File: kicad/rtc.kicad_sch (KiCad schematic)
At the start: 6 parts, among them U1007 AM1805, Y1004 Crystal

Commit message: unify module and board
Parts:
- renumbered C1040 to C37, C1041 to C38, C1042 to C39, C1043 to C40, U1007 to U12, Y1004 to Y2
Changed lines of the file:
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@@
 		(dnp no)
 		(fields_autoplaced yes)
-		(property "Reference" "C1041"
+		(property "Reference" "C38"
 			(at 117.221 57.5853 0)
 			(effects
@@
 			(project "riotee-module"
 				(path "/e235c9a3-080d-42b7-93df-883e69095a9f/1e27cf53-0710-4019-b3d0-1fa374a39b5a/71a24394-376e-48cc-9057-ddfdf0a39757/0e9955bb-beb0-499a-aac5-d497982d12cc"
-					(reference "C1041")
+					(reference "C38")
 					(unit 1)
 				)
@@
 		(on_board yes)
 		(dnp no)
-		(property "Reference" "C1042"
+		(property "Reference" "C39"
 			(at 107.95 96.52 0)
 			(effects
@@
 			(project "riotee-module"
 				(path "/e235c9a3-080d-42b7-93df-883e69095a9f/1e27cf53-0710-4019-b3d0-1fa374a39b5a/71a24394-376e-48cc-9057-ddfdf0a39757/0e9955bb-beb0-499a-aac5-d497982d12cc"
-					(reference "C1042")
+					(reference "C39")
 					(unit 1)
 				)
@@
 		(dnp no)
 		(fields_autoplaced yes)
-		(property "Reference" "C1043"
+		(property "Reference" "C40"
 			(at 180.721 57.5853 0)
 			(effects
@@
 			(project "riotee-module"
 				(path "/e235c9a3-080d-42b7-93df-883e69095a9f/1e27cf53-0710-4019-b3d0-1fa374a39b5a/71a24394-376e-48cc-9057-ddfdf0a39757/0e9955bb-beb0-499a-aac5-d497982d12cc"
-					(reference "C1043")
+					(reference "C40")
 					(unit 1)
 				)
@@
 		(dnp no)
 		(fields_autoplaced yes)
-		(property "Reference" "C1040"
+		(property "Reference" "C37"
 			(at 105.791 57.5853 0)
 			(effects
@@
 			(project "riotee-module"
 				(path "/e235c9a3-080d-42b7-93df-883e69095a9f/1e27cf53-0710-4019-b3d0-1fa374a39b5a/71a24394-376e-48cc-9057-ddfdf0a39757/0e9955bb-beb0-499a-aac5-d497982d12cc"
-					(reference "C1040")
+					(reference "C37")
 					(unit 1)
 				)
@@
 		(dnp no)
 		(fields_autoplaced yes)
-		(property "Reference" "#PWR01048"
+		(property "Reference" "#PWR078"
 			(at 170.18 120.65 0)
 			(effects
@@
 			(project "riotee-module"
 				(path "/e235c9a3-080d-42b7-93df-883e69095a9f/1e27cf53-0710-4019-b3d0-1fa374a39b5a/71a24394-376e-48cc-9057-ddfdf0a39757/0e9955bb-beb0-499a-aac5-d497982d12cc"
-					(reference "#PWR01048")
+					(reference "#PWR078")
 					(unit 1)
 				)
@@
 		(dnp no)
 		(fields_autoplaced yes)
-		(property "Reference" "U1007"
+		(property "Reference" "U12"
 			(at 147.32 54.8472 0)
 			(effects
@@
 			(project "riotee-module"
 				(path "/e235c9a3-080d-42b7-93df-883e69095a9f/1e27cf53-0710-4019-b3d0-1fa374a39b5a/71a24394-376e-48cc-9057-ddfdf0a39757/0e9955bb-beb0-499a-aac5-d497982d12cc"
-					(reference "U1007")
+					(reference "U12")
 					(unit 1)
 				)
@@
 		(on_board yes)
 		(dnp no)
-		(property "Reference" "Y1004"
+		(property "Reference" "Y2"
 			(at 110.9726 82.4484 90)
 			(effects
@@
 			(project "riotee-module"
 				(path "/e235c9a3-080d-42b7-93df-883e69095a9f/1e27cf53-0710-4019-b3d0-1fa374a39b5a/71a24394-376e-48cc-9057-ddfdf0a39757/0e9955bb-beb0-499a-aac5-d497982d12cc"
-					(reference "Y1004")
+					(reference "Y2")
 					(unit 1)
 				)
@@
 		(dnp no)
 		(fields_autoplaced yes)
-		(property "Reference" "#PWR01049"
+		(property "Reference" "#PWR079"
 			(at 177.8 71.12 0)
 			(effects
@@
 			(project "riotee-module"
 				(path "/e235c9a3-080d-42b7-93df-883e69095a9f/1e27cf53-0710-4019-b3d0-1fa374a39b5a/71a24394-376e-48cc-9057-ddfdf0a39757/0e9955bb-beb0-499a-aac5-d497982d12cc"
-					(reference "#PWR01049")
+					(reference "#PWR079")
 					(unit 1)
 				)
@@
 		(dnp no)
 		(fields_autoplaced yes)
-		(property "Reference" "#PWR01045"
+		(property "Reference" "#PWR075"
 			(at 114.3 73.66 0)
 			(effects
@@
 			(project "riotee-module"
 				(path "/e235c9a3-080d-42b7-93df-883e69095a9f/1e27cf53-0710-4019-b3d0-1fa374a39b5a/71a24394-376e-48cc-9057-ddfdf0a39757/0e9955bb-beb0-499a-aac5-d497982d12cc"
-					(reference "#PWR01045")
+					(reference "#PWR075")
 					(unit 1)
 				)
@@
 		(dnp no)
 		(fields_autoplaced yes)
-		(property "Reference" "#PWR01047"
+		(property "Reference" "#PWR077"
 			(at 124.46 120.65 0)
 			(effects
@@
 			(project "riotee-module"
 				(path "/e235c9a3-080d-42b7-93df-883e69095a9f/1e27cf53-0710-4019-b3d0-1fa374a39b5a/71a24394-376e-48cc-9057-ddfdf0a39757/0e9955bb-beb0-499a-aac5-d497982d12cc"
-					(reference "#PWR01047")
+					(reference "#PWR077")
 					(unit 1)
 				)
@@
 		(dnp no)
 		(fields_autoplaced yes)
-		(property "Reference" "#PWR01046"
+		(property "Reference" "#PWR076"
 			(at 114.3 120.65 0)
 			(effects
@@
 			(project "riotee-module"
 				(path "/e235c9a3-080d-42b7-93df-883e69095a9f/1e27cf53-0710-4019-b3d0-1fa374a39b5a/71a24394-376e-48cc-9057-ddfdf0a39757/0e9955bb-beb0-499a-aac5-d497982d12cc"
-					(reference "#PWR01046")
-					(unit 1)
-				)
+					(reference "#PWR076")
+					(unit 1)
+				)

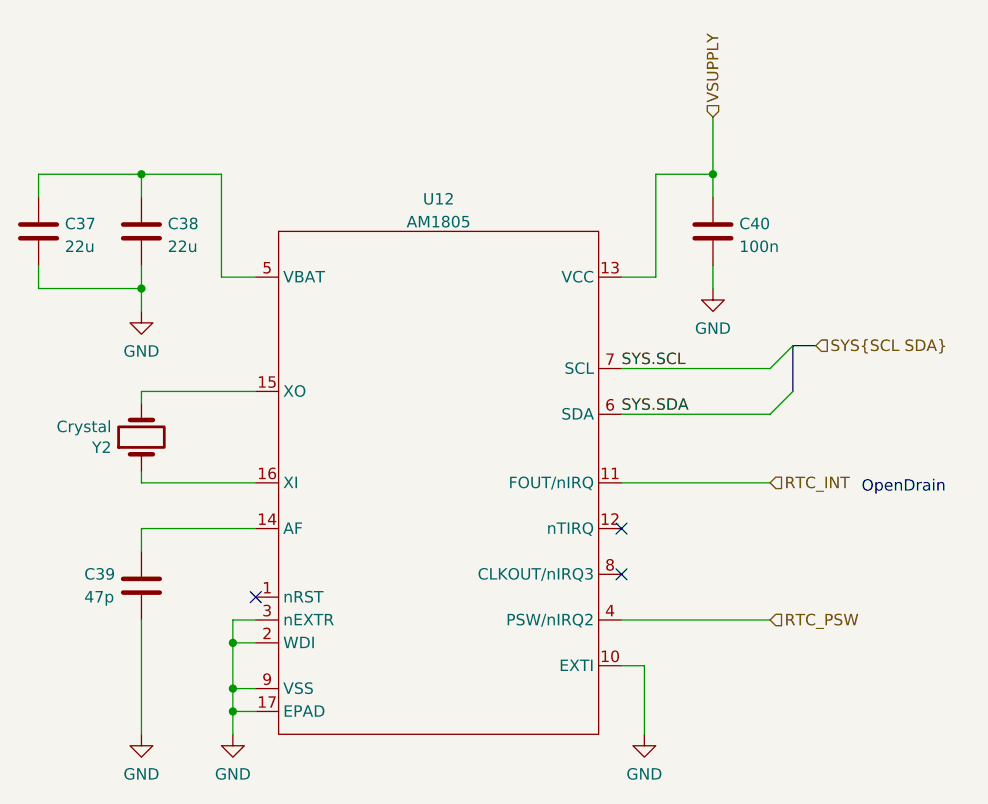
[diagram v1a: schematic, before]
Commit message: move module parts to common library
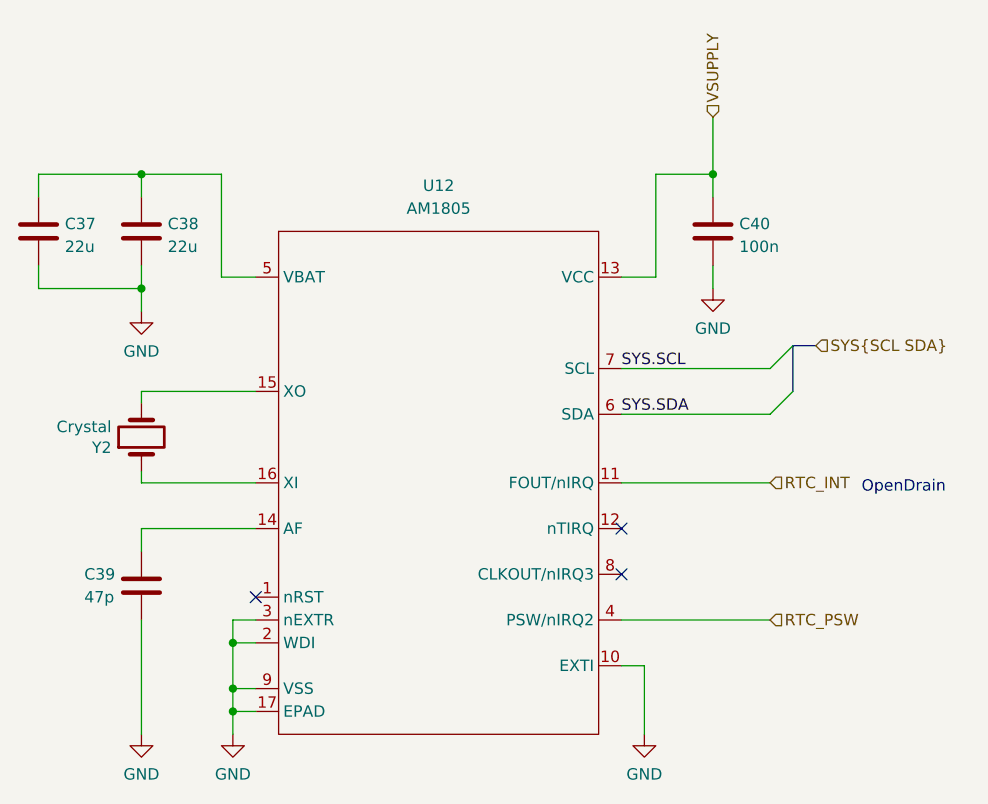
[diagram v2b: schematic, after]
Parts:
- U12: symbol Riotee:AM1805 -> riotee:AM1805
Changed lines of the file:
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@@
 	)
 	(symbol
-		(lib_id "Riotee:AM1805")
+		(lib_id "riotee:AM1805")
 		(at 147.32 86.36 0)
 		(unit 1)
@@
 		(fields_autoplaced yes)
 		(property "Reference" "U12"
-			(at 147.32 54.8472 0)
+			(at 147.32 53.34 0)
 			(effects
 				(font
@@
 		)
 		(property "Value" "AM1805"
-			(at 147.32 57.3841 0)
+			(at 147.32 55.88 0)
 			(effects
 				(font

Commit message: resolve ERC
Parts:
- C37, C38: footprint Riotee:C_0402_1005Metric -> riotee:C_0402_1005Metric
- C39, C40: footprint Riotee:C_0201_0603Metric -> riotee:C_0201_0603Metric
- U12: footprint Riotee:AM_QFN16 -> riotee:AM_QFN16
- Y2: footprint Riotee:ECX-12R -> riotee:ECX-12R
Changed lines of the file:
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@@
 			)
 		)
-		(property "Footprint" "Riotee:C_0402_1005Metric"
+		(property "Footprint" "riotee:C_0402_1005Metric"
 			(at 115.2652 62.23 0)
 			(effects
@@
 			)
 		)
-		(property "Footprint" "Riotee:C_0201_0603Metric"
+		(property "Footprint" "riotee:C_0201_0603Metric"
 			(at 115.2652 101.6 0)
 			(effects
@@
 			)
 		)
-		(property "Footprint" "Riotee:C_0201_0603Metric"
+		(property "Footprint" "riotee:C_0201_0603Metric"
 			(at 178.7652 62.23 0)
 			(effects
@@
 			)
 		)
-		(property "Footprint" "Riotee:C_0402_1005Metric"
+		(property "Footprint" "riotee:C_0402_1005Metric"
 			(at 103.8352 62.23 0)
 			(effects
@@
 			)
 		)
-		(property "Footprint" "Riotee:AM_QFN16"
+		(property "Footprint" "riotee:AM_QFN16"
 			(at 147.32 121.92 0)
 			(effects
@@
 			)
 		)
-		(property "Footprint" "Riotee:ECX-12R"
+		(property "Footprint" "riotee:ECX-12R"
 			(at 114.3 81.28 0)
 			(effects

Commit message: resolve remaining import errors
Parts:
- C37, C38: footprint riotee:C_0402_1005Metric -> Capacitor_SMD:C_0402_1005Metric
- C39, C40: footprint riotee:C_0201_0603Metric -> Capacitor_SMD:C_0201_0603Metric
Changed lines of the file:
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@@
 			)
 		)
-		(property "Footprint" "riotee:C_0402_1005Metric"
+		(property "Footprint" "Capacitor_SMD:C_0402_1005Metric"
 			(at 115.2652 62.23 0)
 			(effects
@@
 			)
 		)
-		(property "Footprint" "riotee:C_0201_0603Metric"
+		(property "Footprint" "Capacitor_SMD:C_0201_0603Metric"
 			(at 115.2652 101.6 0)
 			(effects
@@
 			)
 		)
-		(property "Footprint" "riotee:C_0201_0603Metric"
+		(property "Footprint" "Capacitor_SMD:C_0201_0603Metric"
 			(at 178.7652 62.23 0)
 			(effects
@@
 			)
 		)
-		(property "Footprint" "riotee:C_0402_1005Metric"
+		(property "Footprint" "Capacitor_SMD:C_0402_1005Metric"
 			(at 103.8352 62.23 0)
 			(effects
